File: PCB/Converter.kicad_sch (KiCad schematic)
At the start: 91 parts, among them Q1 ${MFGPN}, Q12 HUASHUO HSBB0115, Q2 ${MFGPN}, Q3 ${MFGPN}, Q4 ${MFGPN}, Q5 HUASHUO HSBB0115, U1 LT8390AIUFD-PBF

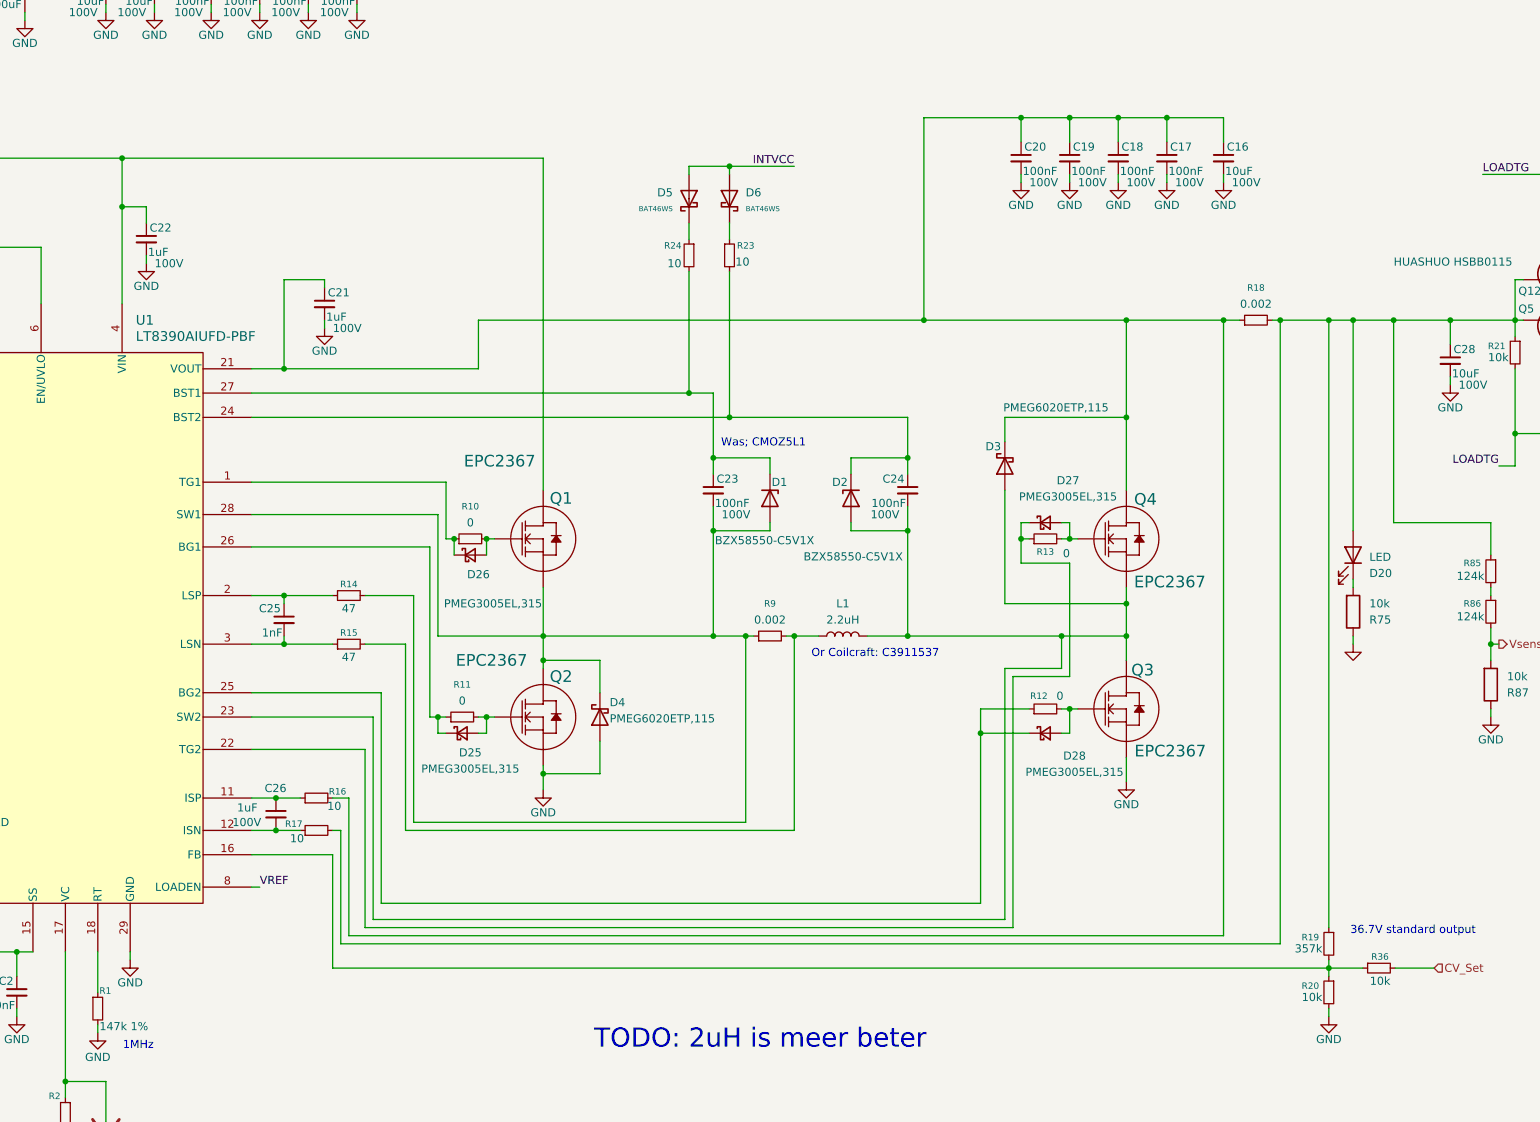
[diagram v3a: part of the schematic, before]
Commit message: Added testpoints
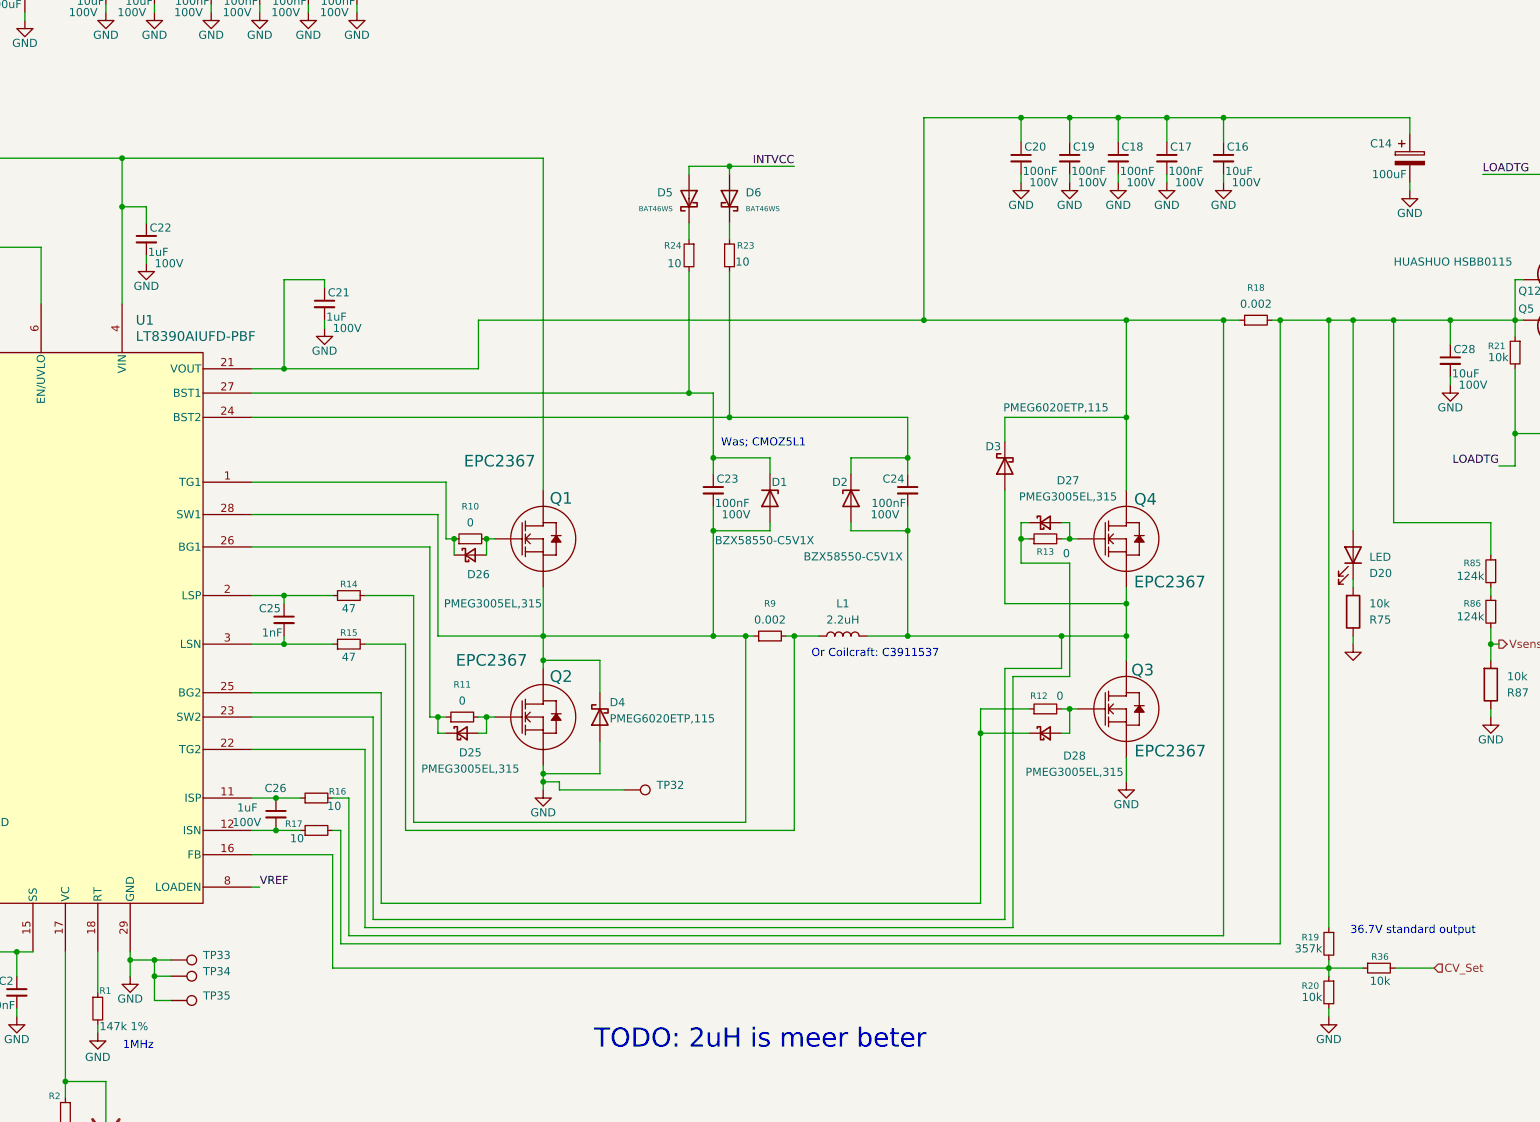
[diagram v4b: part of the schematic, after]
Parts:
- added C14: 100uF, Capacitor_SMD:CP_Elec_10x12.6, symbol Device:C_Polarized
- added TP32, TP33, TP34, TP35: tp_round_70, TestPoint:TestPoint_Pad_D1.0mm, symbol Connector:TestPoint
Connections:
- net GND: now also C14.2, TP32.1, TP33.1, TP34.1, TP35.1
- net at C16.1, C17.1, C18.1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: now also C14.1

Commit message: BOM: R5 CTRL divider 124k -> 357k (fail-safe current limit default)
- R5 biases the LT8390A CTRL pin: DAC-float default current limit drops
  from ~25A to ~5A, so a MCU brown-out/boot glitch can no longer demand
  the inductor's full rating. Full 0-50A range via CC DAC is unchanged.
- LCSC/JLC fields: C36777 -> C27005 (UNI-ROYAL 0402WGF3573TCE, 357k 1%,
  same part as R19/R7)
- Fit R3 = 100k (SS-VREF strap): short-circuit fault mode changes from
  hiccup to keep-running (done in KiCad)
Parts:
- R3: value (none) -> 100k; now fitted
- R5: value 124k -> 357k; JLC (none) -> C27005; LCSC C36777 -> C27005
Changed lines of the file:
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@@
 			)
 		)
-		(property "Value" "124k"
+		(property "Value" "357k"
 			(at 90.424 134.112 0)
 			(show_name no)
@@
 			)
 		)
-		(property "LCSC" "C36777"
+		(property "LCSC" "C27005"
+			(at 89.916 132.08 0)
+			(hide yes)
+			(show_name no)
+			(do_not_autoplace no)
+			(effects
+				(font
+					(size 1.27 1.27)
+				)
+			)
+		)
+		(property "JLC" "C27005"
 			(at 89.916 132.08 0)
 			(hide yes)
@@
 		(on_board yes)
 		(in_pos_files yes)
-		(dnp yes)
+		(dnp no)
 		(property "Reference" "R3"
 			(at 113.03 192.532 90)
@@
 			)
 		)
-		(property "Value" ""
+		(property "Value" "100k"
 			(at 113.538 196.088 90)
 			(show_name no)

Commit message: EPR sort of works with some chargers
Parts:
- removed R75: 10k, Resistor_SMD:R_0402_1005Metric, symbol Device:R
- added R75: 75k, Resistor_SMD:R_0402_1005Metric, symbol Device:R_Small
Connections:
- net GND: now also R75.2
- net at D20.1 (K): now also R75.1
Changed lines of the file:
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@@
 	(wire
 		(pts
-			(xy 328.93 146.05) (xy 328.93 144.78)
+			(xy 328.93 143.51) (xy 328.93 146.05)
 		)
 		(stroke
@@
 	(wire
 		(pts
-			(xy 328.93 135.89) (xy 328.93 137.16)
+			(xy 328.93 135.89) (xy 328.93 138.43)
 		)
 		(stroke
@@
 	)
 	(symbol
+		(lib_id "Device:R_Small")
+		(at 328.93 140.97 0)
+		(mirror y)
+		(unit 1)
+		(body_style 1)
+		(exclude_from_sim no)
+		(in_bom yes)
+		(on_board yes)
+		(in_pos_files yes)
+		(dnp no)
+		(property "Reference" "R75"
+			(at 327.406 139.954 0)
+			(show_name no)
+			(do_not_autoplace no)
+			(effects
+				(font
+					(size 1.016 1.016)
+				)
+				(justify left)
+			)
+		)
+		(property "Value" "75k"
+			(at 327.914 141.732 0)
+			(show_name no)
+			(do_not_autoplace no)
+			(effects
+				(font
+					(size 1.27 1.27)
+				)
+				(justify left)
+			)
+		)
+		(property "Footprint" "Resistor_SMD:R_0402_1005Metric"
+			(at 328.93 140.97 0)
+			(hide yes)
+			(show_name no)
+			(do_not_autoplace no)
+			(effects
+				(font
+					(size 1.27 1.27)
+				)
+			)
+		)
+		(property "Datasheet" ""
+			(at 328.93 140.97 0)
+			(hide yes)
+			(show_name no)
+			(do_not_autoplace no)
+			(effects
+				(font
+					(size 1.27 1.27)
+				)
+			)
+		)
+		(property "Description" "Resistor, small symbol"
+			(at 328.93 140.97 0)
+			(hide yes)
+			(show_name no)
+			(do_not_autoplace no)
+			(effects
+				(font
+					(size 1.27 1.27)
+				)
+			)
+		)
+		(property "LCSC" "C25798"
+			(at 327.406 139.954 0)
+			(hide yes)
+			(show_name no)
+			(do_not_autoplace no)
+			(effects
+				(font
+					(size 1.27 1.27)
+				)
+			)
+		)
+		(pin "1"
+		)
+		(pin "2"
+		)
+		(instances
+			(project "nitride-nano"
+				(path "/aaad0350-e7db-44d5-b7ef-99e6416f6948/f0962043-1aad-4f17-a8f7-b50910365543"
+					(reference "R75")
+					(unit 1)
+				)
+			)
+		)
+	)
+	(symbol
 		(lib_id "Device:Q_PMOS")
 		(at 360.68 86.36 270)
@@
 					(unit 1)
 				)
-			)
-		)
-	)
-	(symbol
-		(lib_id "Device:R")
-		(at 328.93 140.97 0)
-		(mirror x)
-		(unit 1)
-		(body_style 1)
-		(exclude_from_sim no)
-		(in_bom yes)
-		(on_board yes)
-		(in_pos_files yes)
-		(dnp no)
-		(fields_autoplaced yes)
-		(property "Reference" "R75"
-			(at 331.47 142.2401 0)
-			(show_name no)
-			(do_not_autoplace no)
-			(effects
-				(font
-					(size 1.27 1.27)
-				)
-				(justify left)
-			)
-		)
-		(property "Value" "10k"
-			(at 331.47 139.7001 0)
-			(show_name no)
-			(do_not_autoplace no)
-			(effects
-				(font
-					(size 1.27 1.27)
-				)
-				(justify left)
-			)
-		)
-		(property "Footprint" "Resistor_SMD:R_0402_1005Metric"
-			(at 327.152 140.97 90)
-			(hide yes)
-			(show_name no)
-			(do_not_autoplace no)
-			(effects
-				(font
-					(size 1.27 1.27)
-				)
-			)
-		)
-		(property "Datasheet" ""
-			(at 328.93 140.97 0)
-			(hide yes)
-			(show_name no)
-			(do_not_autoplace no)
-			(effects
-				(font
-					(size 1.27 1.27)
-				)
-			)
-		)
-		(property "Description" "Resistor"
-			(at 328.93 140.97 0)
-			(hide yes)
-			(show_name no)
-			(do_not_autoplace no)
-			(effects
-				(font
-					(size 1.27 1.27)
-				)
-			)
-		)
-		(property "LCSC" "C2906861"
-			(at 331.47 142.2401 0)
-			(hide yes)
-			(show_name no)
-			(do_not_autoplace no)
-			(effects
-				(font
-					(size 1.27 1.27)
-				)
-			)
-		)
-		(pin "2"
-		)
-		(pin "1"
-		)
-		(instances
-			(project "nitride-nano"
-				(path "/aaad0350-e7db-44d5-b7ef-99e6416f6948/f0962043-1aad-4f17-a8f7-b50910365543"
-					(reference "R75")
-					(unit 1)
-				)

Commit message: Added NMOS output switch (rated for 20A this time)
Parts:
- removed Q12, Q5: HUASHUO HSBB0115, thommys-parts2:PRPAK-8_L3.0-W3.0-P0.65-BL-EP, symbol Device:Q_PMOS
- removed R57: 3.3, Resistor_SMD:R_0402_1005Metric, symbol Device:R_Small
- added D11: BZT52C4V7S, PCM_JLCPCB:D_SOD-323, symbol PCM_JLCPCB-Diodes:Zener,BZT52C4V7S
- added Q12: AO3400A, PCM_JLCPCB:Q_SOT-23, symbol PCM_JLCPCB-Transistors:NMOS,AO3400A
- added Q5: ${MFGPN}, thommys-parts2:D1068, symbol Thommys-parts2:EPC2367
- added Q7: AO3401A, PCM_JLCPCB:Q_SOT-23, symbol PCM_JLCPCB-Transistors:PMOS,AO3401A
- added R57: 4.7k 1%, Resistor_SMD:R_0402_1005Metric, symbol 0_passives:R_0402
- added R58: 27R 1%, Resistor_SMD:R_0402_1005Metric, symbol 0_passives:R_0402
- R21: value 10k -> 100k; LCSC C2906861 -> (none)
- R22: value 3.3 -> 100k; LCSC C25165 -> (none)
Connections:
- net +5V: now also R22.2, Q7.2 (S)
- net GND: now also R21.1, D11.2, Q12.2 (S), Q5.2 (S), Q5.4 (S), R57.1
- net at FB5.1, FB6.1, FB7.1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: now also C28.1, D20.2 (A), R17.2, R18.2, R19.1, R85.1
- removed net LOADTG: R21.2, R22.1, U1.20 (LOADTG)
- net PWR_REG_OUT renamed PWR_REG_OUT+
- new net: Q12.3 (D), Q7.1 (G), R22.1
- new net: Q7.3 (D), R58.1
- new net: D11.1, Q5.1 (G), R57.2, R58.2
- new net PWR_G: Q12.1 (G), R21.2
- new net PWR_REG_OUT-: Q5.3 (D), Q5.5 (D)
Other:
- moved on the sheet: C1, C10, C11, C12, C13, C14, C16, C17, C18, C19, C2, C20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
